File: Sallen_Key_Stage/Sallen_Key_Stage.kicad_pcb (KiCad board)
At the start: 4 copper layers, 35.6 x 30.5 mm, 17 parts, among them J1 Conn_01x05_Pin, J2 Conn_01x05_Socket, U2 LM358

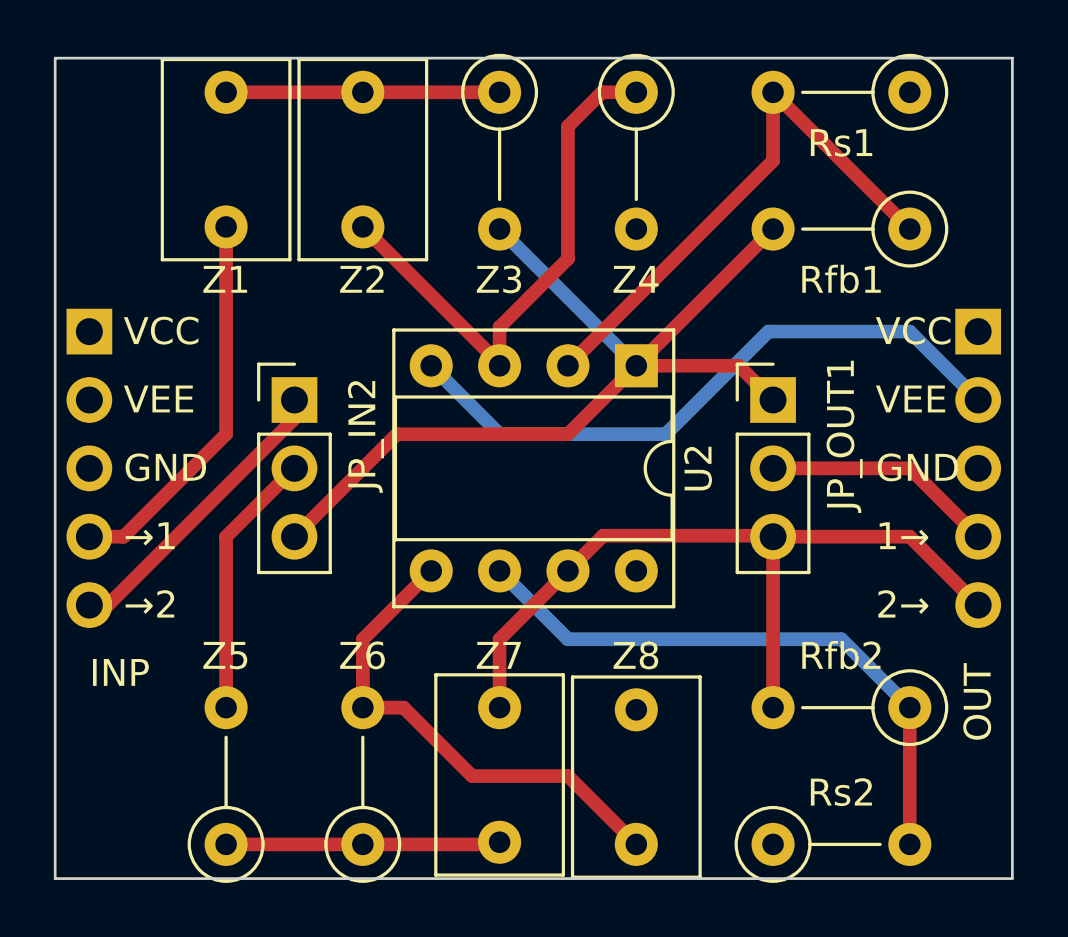
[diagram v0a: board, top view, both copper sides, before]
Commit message: v1.0 of STLink-MIPI-14-to-SWD-10
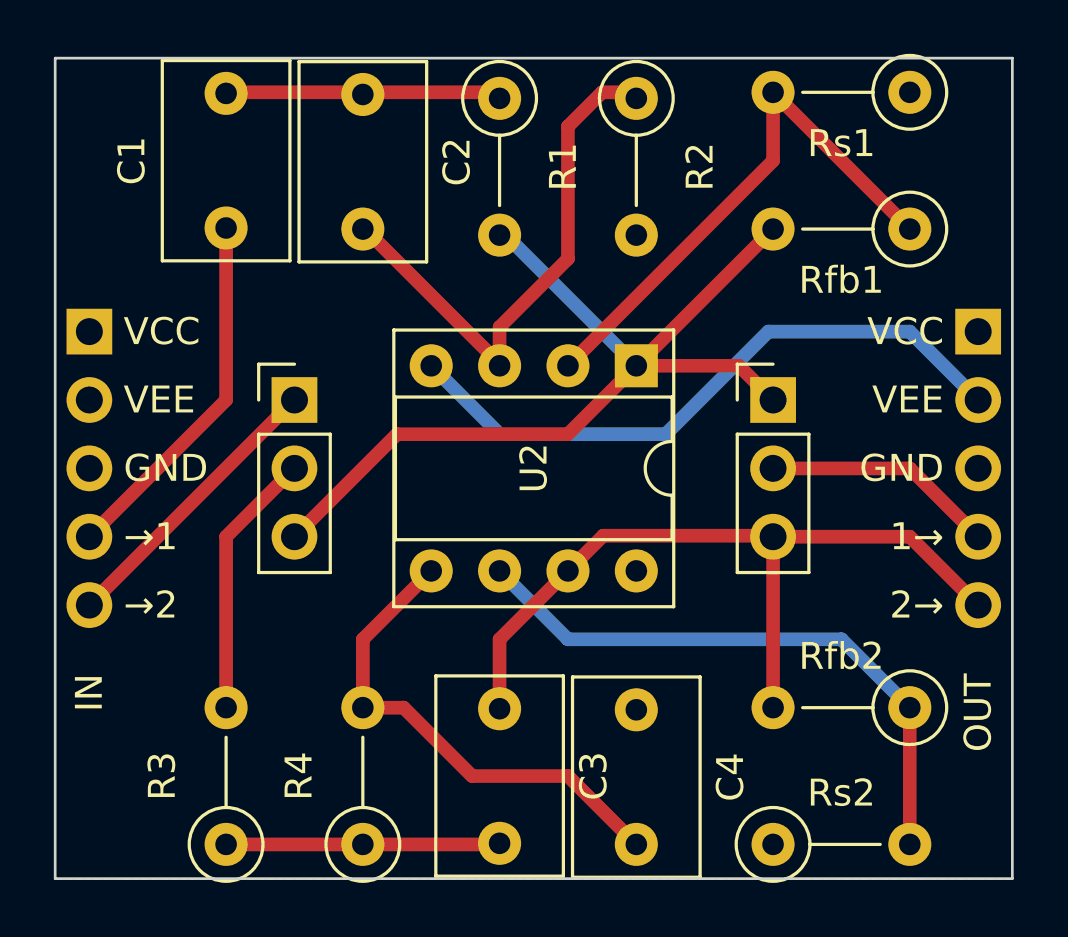
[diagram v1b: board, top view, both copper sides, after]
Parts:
- removed Z1, Z2, Z7, Z8: 10n, Capacitor_THT:C_Rect_L7.2mm_W4.5mm_P5.00mm_FKS2_FKP2_MKS2_MKP2
- removed Z3, Z4, Z5, Z6: 2k, Resistor_THT:R_Axial_DIN0207_L6.3mm_D2.5mm_P5.08mm_Vertical
- added C1: 10n, Capacitor_THT:C_Rect_L7.2mm_W4.5mm_P5.00mm_FKS2_FKP2_MKS2_MKP2, F.Cu at (116.8, 55.8)
- added C2: 10n, Capacitor_THT:C_Rect_L7.2mm_W4.5mm_P5.00mm_FKS2_FKP2_MKS2_MKP2, F.Cu at (121.9, 50.9)
- added C3: 10n, Capacitor_THT:C_Rect_L7.2mm_W4.5mm_P5.00mm_FKS2_FKP2_MKS2_MKP2, F.Cu at (127.0, 73.7)
- added C4: 10n, Capacitor_THT:C_Rect_L7.2mm_W4.5mm_P5.00mm_FKS2_FKP2_MKS2_MKP2, F.Cu at (132.1, 73.7)
- added R1: 2k, Resistor_THT:R_Axial_DIN0207_L6.3mm_D2.5mm_P5.08mm_Vertical, F.Cu at (127.0, 51.0)
- added R2: 2k, Resistor_THT:R_Axial_DIN0207_L6.3mm_D2.5mm_P5.08mm_Vertical, F.Cu at (132.1, 51.0)
- added R3: 2K, Resistor_THT:R_Axial_DIN0207_L6.3mm_D2.5mm_P5.08mm_Vertical, F.Cu at (116.8, 78.7)
- added R4: 2k, Resistor_THT:R_Axial_DIN0207_L6.3mm_D2.5mm_P5.08mm_Vertical, F.Cu at (121.9, 78.7)
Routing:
- net Net-(Z5-Pad1): track 10.2 -> 0.00 mm
- net Net-(Z1-Pad2): track 10.2 -> 0.00 mm
- net Net-(C3-Pad2): track 0.00 -> 10.2 mm
- net Net-(C1-Pad2): track 0.00 -> 10.2 mm
- net IN1: track 14.3 -> 13.5 mm
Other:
- board text added: "(A)"
- board text added: "(B)"
- board text added: "IN"
- board text added: "IN1"
- board text added: "IN2"
- board text added: "OUT1"
- board text added: "OUT1,OUT2"
- board text added: "OUT2"
- board text removed: "INP"
